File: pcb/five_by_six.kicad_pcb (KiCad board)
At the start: 2 copper layers, 156.1 x 98.2 mm, 67 parts, among them SW1 SW_Push, SW10 SW_Push, SW11 SW_Push, SW12 SW_Push, SW13 SW_Push, SW14 SW_Push, SW15 SW_Push, SW16 SW_Push, SW17 SW_Push, SW18 SW_Push, SW19 SW_Push, SW2 SW_Push, SW20 SW_Push, SW21 SW_Push, SW22 SW_Push, SW23 SW_Push, SW24 SW_Push, SW25 SW_Push, SW26 SW_Push, SW27 SW_Push, SW28 SW_Push, SW29 SW_Push, SW3 SW_Push, SW30 SW_Push, SW31 MX, SW4 SW_Push, SW5 SW_Push, SW6 SW_Push, SW7 SW_Push, SW8 SW_Push, SW9 SW_Push, U1 ProMicro, U2 TRRS

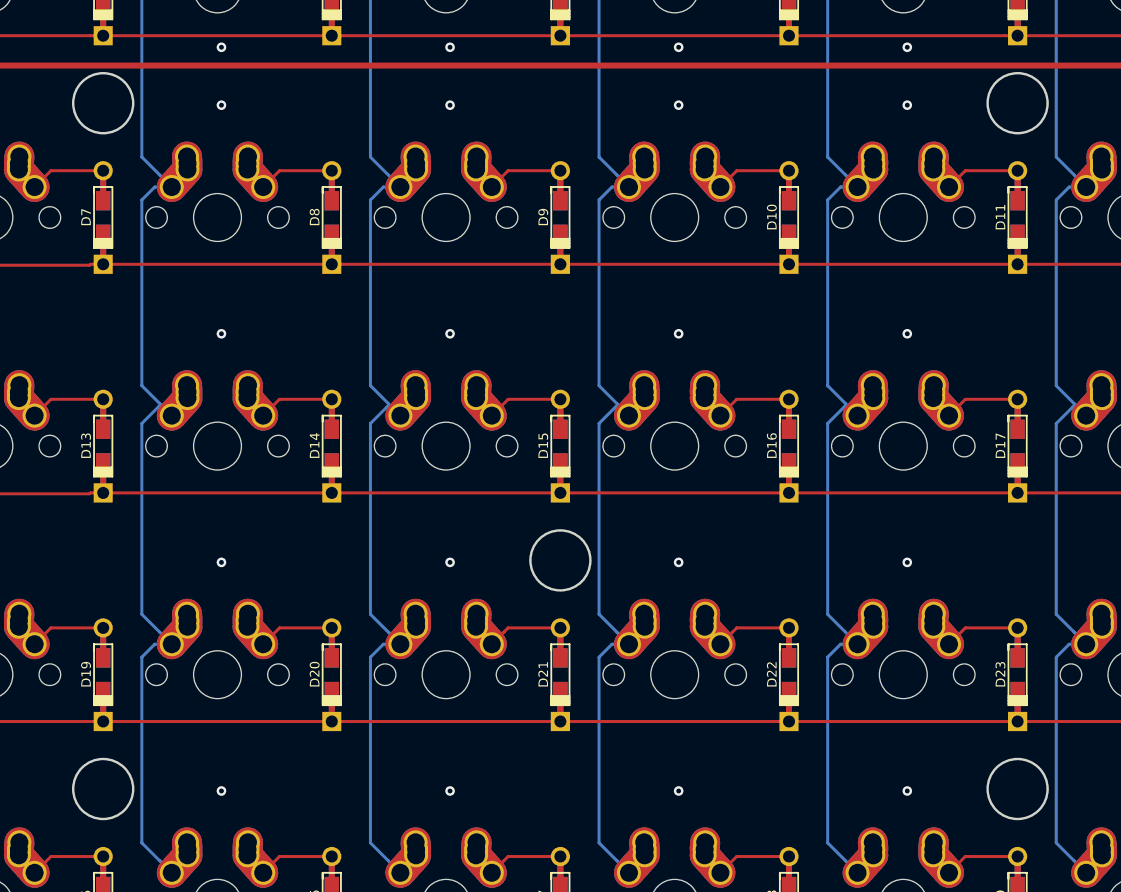
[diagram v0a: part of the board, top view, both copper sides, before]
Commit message: Add mounting holes
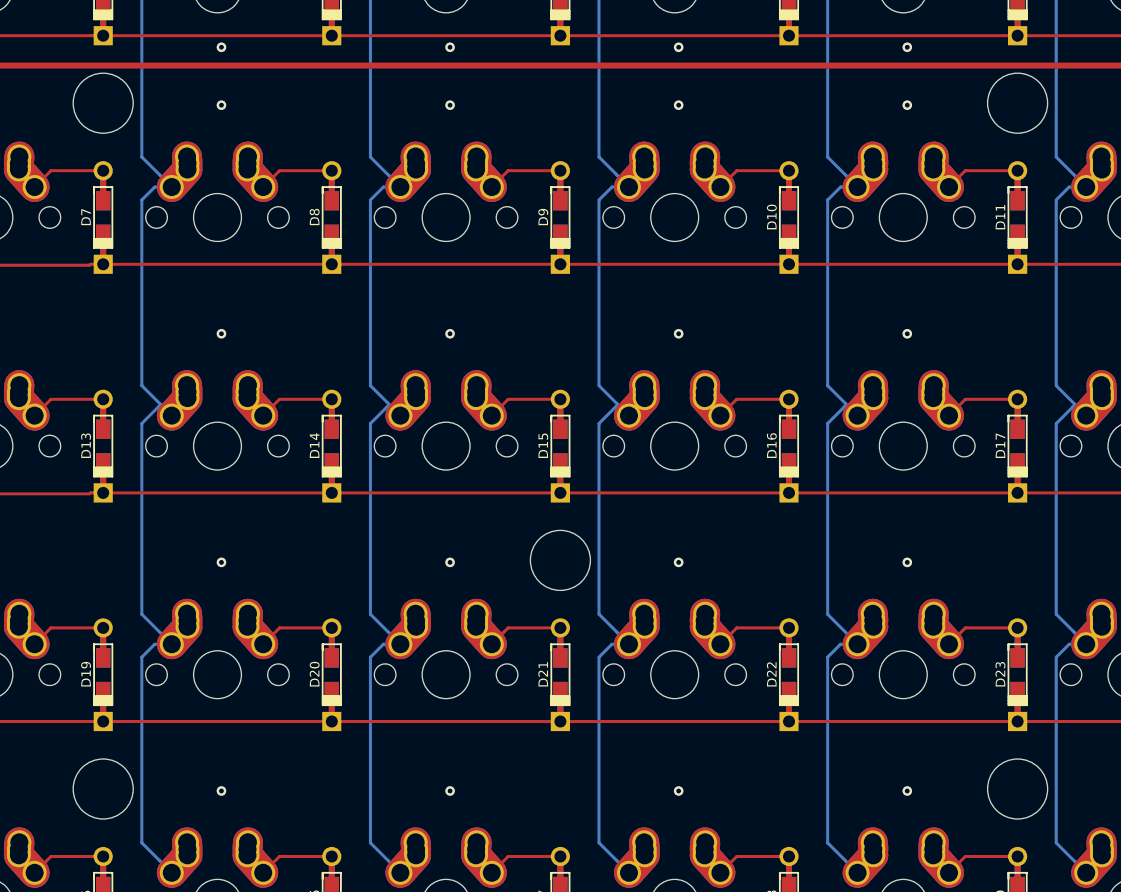
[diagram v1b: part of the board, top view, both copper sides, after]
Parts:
- added REF**: MountingHole_5mm, MountingHole_5mm, F.Cu at (185.7, 59.5)
- added REF**: MountingHole_5mm, MountingHole_5mm, F.Cu at (185.7, 116.7)
- added REF**: MountingHole_5mm, MountingHole_5mm, F.Cu at (109.5, 116.7)
- added REF**: MountingHole_5mm, MountingHole_5mm, F.Cu at (147.6, 97.6)
- added REF**: MountingHole_5mm, MountingHole_5mm, F.Cu at (109.5, 59.5)
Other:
- outline, holes or cut-outs redrawn
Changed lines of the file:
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@@
     (tracks 371)
     (zones 0)
-    (modules 67)
+    (modules 72)
     (nets 49)
   )
@@
     (add_net VCC)
   )
+  (module MountingHole_5mm (layer F.Cu)
+    (at 185.725 59.525)
+    (descr "Mounting Hole 5mm, no annular")
+    (tags "mounting hole 5mm no annular")
+    (attr virtual)
+    (fp_text reference REF** (at 0 -6) (layer F.SilkS) hide
+      (effects (font (size 1 1) (thickness 0.15)))
+    )
+    (fp_text value MountingHole_5mm (at 0 6) (layer F.Fab)
+      (effects (font (size 1 1) (thickness 0.15)))
+    )
+    (fp_circle (center 0 0) (end 5.25 0) (layer F.CrtYd) (width 0.05))
+    (fp_circle (center 0 0) (end 5 0) (layer Cmts.User) (width 0.15))
+    (fp_text user %R (at 0.3 0) (layer F.Fab)
+      (effects (font (size 1 1) (thickness 0.15)))
+    )
+    (pad 1 np_thru_hole circle (at 0 0) (size 5 5) (drill 5) (layers *.Cu *.Mask))
+  )
+  (module MountingHole_5mm (layer F.Cu)
+    (at 185.725 116.675)
+    (descr "Mounting Hole 5mm, no annular")
+    (tags "mounting hole 5mm no annular")
+    (attr virtual)
+    (fp_text reference REF** (at 0 -6) (layer F.SilkS) hide
+      (effects (font (size 1 1) (thickness 0.15)))
+    )
+    (fp_text value MountingHole_5mm (at 0 6) (layer F.Fab)
+      (effects (font (size 1 1) (thickness 0.15)))
+    )
+    (fp_circle (center 0 0) (end 5.25 0) (layer F.CrtYd) (width 0.05))
+    (fp_circle (center 0 0) (end 5 0) (layer Cmts.User) (width 0.15))
+    (fp_text user %R (at 0.3 0) (layer F.Fab)
+      (effects (font (size 1 1) (thickness 0.15)))
+    )
+    (pad 1 np_thru_hole circle (at 0 0) (size 5 5) (drill 5) (layers *.Cu *.Mask))
+  )
+  (module MountingHole_5mm (layer F.Cu)
+    (at 109.525 116.675)
+    (descr "Mounting Hole 5mm, no annular")
+    (tags "mounting hole 5mm no annular")
+    (attr virtual)
+    (fp_text reference REF** (at 0 -6) (layer F.SilkS) hide
+      (effects (font (size 1 1) (thickness 0.15)))
+    )
+    (fp_text value MountingHole_5mm (at 0 6) (layer F.Fab)
+      (effects (font (size 1 1) (thickness 0.15)))
+    )
+    (fp_circle (center 0 0) (end 5.25 0) (layer F.CrtYd) (width 0.05))
+    (fp_circle (center 0 0) (end 5 0) (layer Cmts.User) (width 0.15))
+    (fp_text user %R (at 0.3 0) (layer F.Fab)
+      (effects (font (size 1 1) (thickness 0.15)))
+    )
+    (pad 1 np_thru_hole circle (at 0 0) (size 5 5) (drill 5) (layers *.Cu *.Mask))
+  )
+  (module MountingHole_5mm (layer F.Cu)
+    (at 147.625 97.625)
+    (descr "Mounting Hole 5mm, no annular")
+    (tags "mounting hole 5mm no annular")
+    (attr virtual)
+    (fp_text reference REF** (at 0 -6) (layer F.SilkS) hide
+      (effects (font (size 1 1) (thickness 0.15)))
+    )
+    (fp_text value MountingHole_5mm (at 0 6) (layer F.Fab)
+      (effects (font (size 1 1) (thickness 0.15)))
+    )
+    (fp_circle (center 0 0) (end 5.25 0) (layer F.CrtYd) (width 0.05))
+    (fp_circle (center 0 0) (end 5 0) (layer Cmts.User) (width 0.15))
+    (fp_text user %R (at 0.3 0) (layer F.Fab)
+      (effects (font (size 1 1) (thickness 0.15)))
+    )
+    (pad 1 np_thru_hole circle (at 0 0) (size 5 5) (drill 5) (layers *.Cu *.Mask))
+  )
+  (module MountingHole_5mm (layer F.Cu)
+    (at 109.525 59.525)
+    (descr "Mounting Hole 5mm, no annular")
+    (tags "mounting hole 5mm no annular")
+    (attr virtual)
+    (fp_text reference REF** (at 0 -6) (layer F.SilkS) hide
+      (effects (font (size 1 1) (thickness 0.15)))
+    )
+    (fp_text value MountingHole_5mm (at 0 6) (layer F.Fab)
+      (effects (font (size 1 1) (thickness 0.15)))
+    )
+    (fp_circle (center 0 0) (end 5.25 0) (layer F.CrtYd) (width 0.05))
+    (fp_circle (center 0 0) (end 5 0) (layer Cmts.User) (width 0.15))
+    (fp_text user %R (at 0.3 0) (layer F.Fab)
+      (effects (font (size 1 1) (thickness 0.15)))
+    )
+    (pad 1 np_thru_hole circle (at 0 0) (size 5 5) (drill 5) (layers *.Cu *.Mask))
+  )
   (module Button_Switch_THT:SW_PUSH_6mm_H7.3mm (layer F.Cu)
     (at 77.47 78.105 315)
@@
   )
   (gr_arc (start 218.25 54.600505) (end 218.25 56.600505) (angle -90) (layer Edge.Cuts) (width 0.2))
-  (gr_circle (center 109.525 59.525) (end 112.025 59.525) (layer Edge.Cuts) (width 0.2))
-  (gr_circle (center 147.625 97.625) (end 150.125 97.625) (layer Edge.Cuts) (width 0.2))
-  (gr_circle (center 109.525 116.675) (end 112.025 116.675) (layer Edge.Cuts) (width 0.2))
-  (gr_circle (center 185.725 116.675) (end 188.225 116.675) (layer Edge.Cuts) (width 0.2))
-  (gr_circle (center 185.725 59.525) (end 188.225 59.525) (layer Edge.Cuts) (width 0.2))
+  (gr_circle (center 109.525 59.525) (end 112.025 59.525) (layer Eco1.User) (width 0.2))
+  (gr_circle (center 147.625 97.625) (end 150.125 97.625) (layer Eco1.User) (width 0.2))
+  (gr_circle (center 109.525 116.675) (end 112.025 116.675) (layer Eco1.User) (width 0.2))
+  (gr_circle (center 185.725 116.675) (end 188.225 116.675) (layer Eco1.User) (width 0.2))
+  (gr_circle (center 185.725 59.525) (end 188.225 59.525) (layer Eco1.User) (width 0.2))
   (gr_arc (start 66.15 41) (end 66.15 39) (angle -90) (layer Edge.Cuts) (width 0.2))
   (gr_line (start 64.15 75.795732) (end 64.15 41) (layer Edge.Cuts) (width 0.2))
